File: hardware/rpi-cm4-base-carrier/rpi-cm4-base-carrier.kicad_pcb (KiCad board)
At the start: 4 copper layers, 129.5 x 61.3 mm, 66 parts, among them J1 690-019-298-412, J2 DNP, J3 USB4105-GF-A, J4 SM04B-SRSS-TB(LF)(SN), J5 THD-02-R, J6 Micro_SD_Card_Det, J7 USB_OTG, J8 690-008-221-904, J9 Conn_02x05_Odd_Even, U1 RT9742SNGV, U10 AP22653W6, U2 74LVC1G07SE-7, U3 TPD4EUSB30, U4 TPD4EUSB30, U5 MagJack-A70-112-331N126, U6 RT9742GGJ5, U7 FSUSB42MUX, U8 USB2514B-I/M2, U9 TPD4EUSB30, Y1 CX3225CA24000D0HSSCC

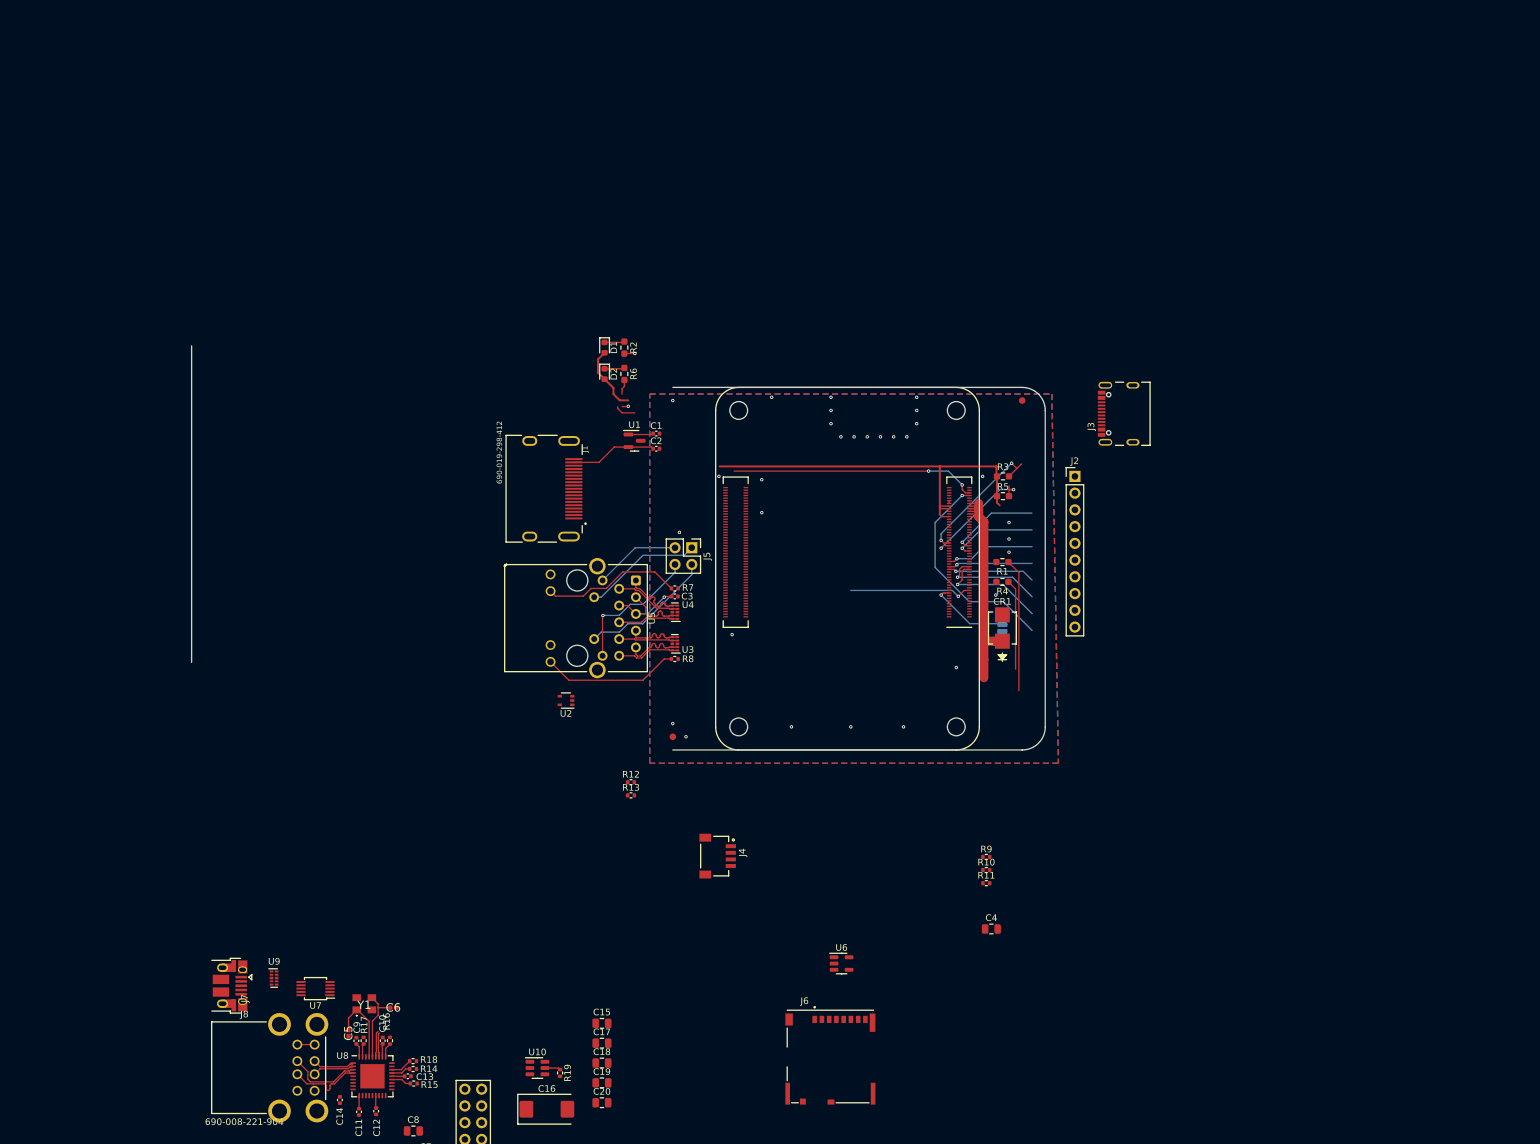
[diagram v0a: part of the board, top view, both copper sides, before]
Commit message: addition of 4xRGB LED's and I2C driver, also includes right angle lightpipe
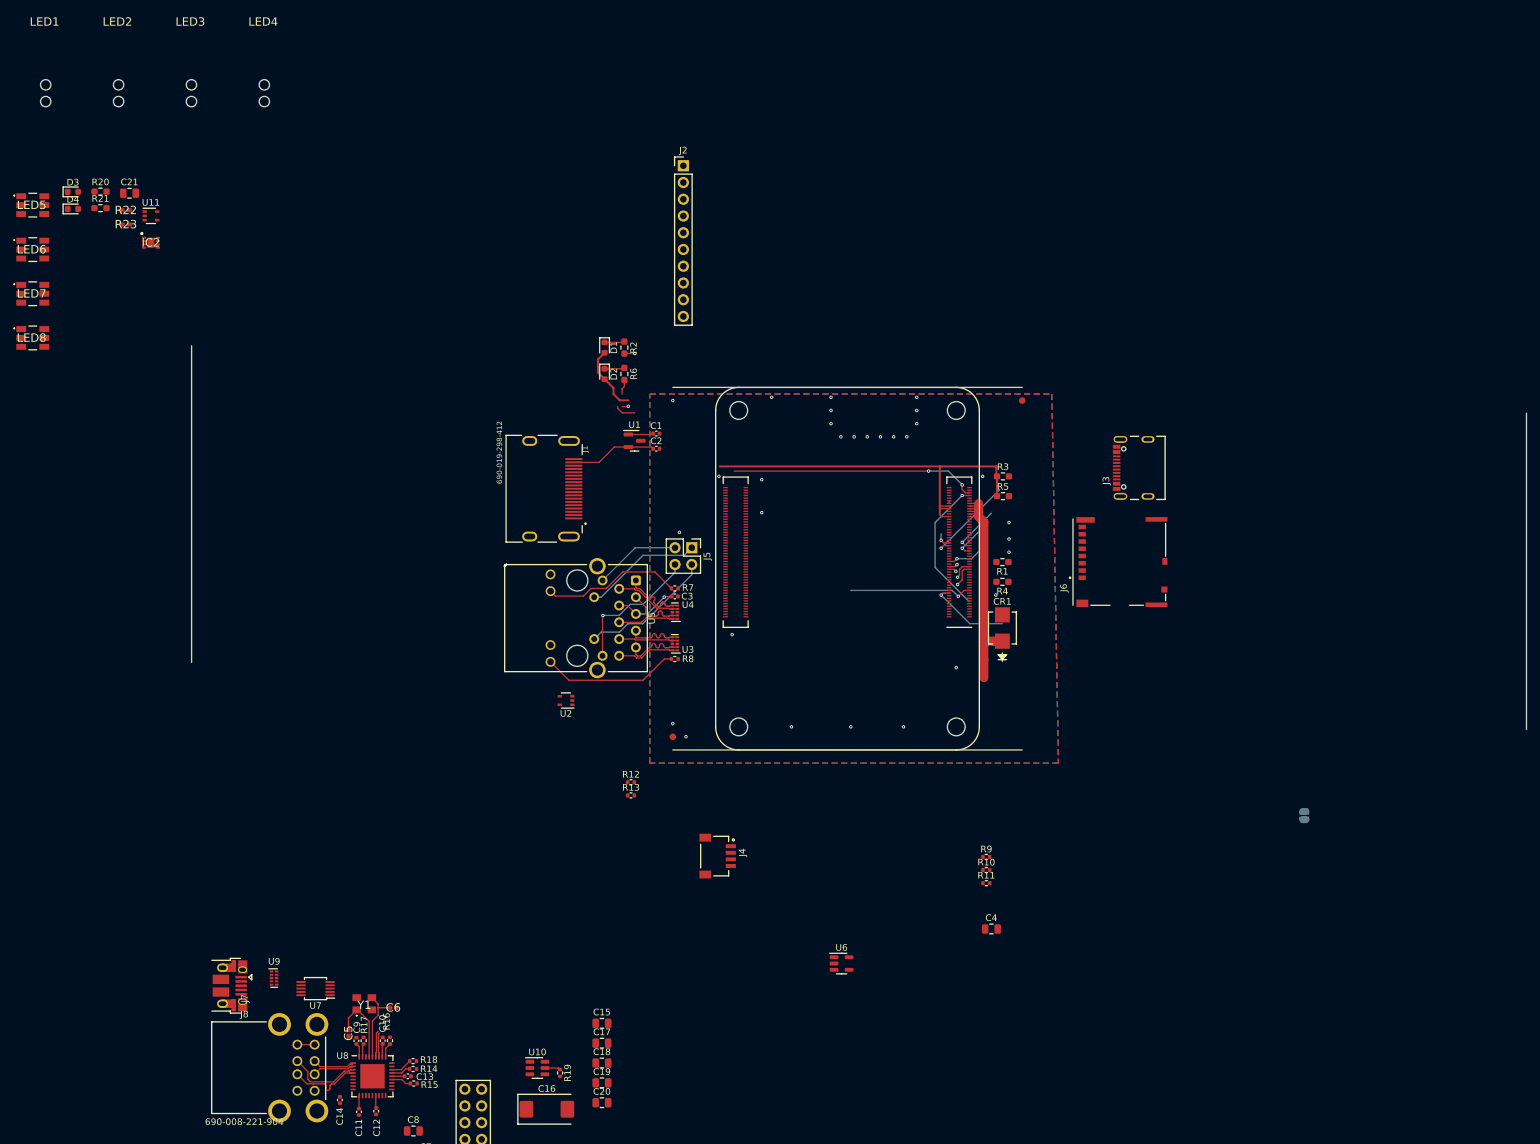
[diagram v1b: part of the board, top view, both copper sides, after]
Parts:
- added C21: 10u, Capacitor_SMD:C_0805_2012Metric, F.Cu at (37.1, 47.5)
- added D3: LED Green, LED_SMD:LED_0603_1608Metric, F.Cu at (28.5, 47.3)
- added D4: LED Red, LED_SMD:LED_0603_1608Metric, F.Cu at (28.5, 49.9)
- added IC2: KTD2052BEVAA-TR, SamacSys_Parts:SON50P200X200X58-9N, F.Cu at (40.3, 55.1)
- added LED1: 515-1114F, SamacSys_Parts:515-1114F, F.Cu at (25.1, 45.3)
- added LED2: 515-1114F, SamacSys_Parts:515-1114F, F.Cu at (36.2, 45.3)
- added LED3: 515-1114F, SamacSys_Parts:515-1114F, F.Cu at (47.2, 45.3)
- added LED4: 515-1114F, SamacSys_Parts:515-1114F, F.Cu at (58.3, 45.3)
- added LED5: APF3236SEEZGKQBKC, SamacSys_Parts:APF3236SEEZGKQBKC, F.Cu at (22.4, 49.4)
- added LED6: APF3236SEEZGKQBKC, SamacSys_Parts:APF3236SEEZGKQBKC, F.Cu at (22.4, 56.1)
- added LED7: APF3236SEEZGKQBKC, SamacSys_Parts:APF3236SEEZGKQBKC, F.Cu at (22.4, 62.8)
- added LED8: APF3236SEEZGKQBKC, SamacSys_Parts:APF3236SEEZGKQBKC, F.Cu at (22.4, 69.5)
- added R20: 1k, Resistor_SMD:R_0603_1608Metric_Pad0.98x0.95mm_HandSolder, F.Cu at (32.7, 47.3)
- added R21: 1k, Resistor_SMD:R_0603_1608Metric_Pad0.98x0.95mm_HandSolder, F.Cu at (32.7, 49.8)
- added R22: 4K7, SamacSys_Parts:RESC1005X37N, F.Cu at (36.5, 50.1)
- added R23: 4K7, SamacSys_Parts:RESC1005X37N, F.Cu at (36.5, 52.3)
- added U11: 74LVC1G07SE-7, Package_TO_SOT_SMD:SOT-353_SC-70-5, F.Cu at (40.3, 51.0)
- moved J6 86.9 mm to (187.2, 103.5), turned to 90 degrees
- moved J2 75.8 mm to (121.1, 43.4)
- moved JP1 53.9 mm to (215.3, 141.9)
- moved J3 8.52 mm to (191.6, 89.2)
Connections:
- J1 pad 10: /CM4 High Speed/HDMI0_CK_P -> /CM4 High Speed/HDMI0_CK_N
- J1 pad 4: /CM4 High Speed/HDMI0_D1_P -> /CM4 High Speed/HDMI0_CK_N
- J1 pad 7: /CM4 High Speed/HDMI0_D0_P -> /CM4 High Speed/HDMI0_CK_N
- J1 pad 9: /CM4 High Speed/HDMI0_D0_N -> /CM4 High Speed/HDMI0_CK_N
- Module1 pad 176: /CM4 High Speed/HDMI0_D1_P -> /CM4 High Speed/HDMI0_CK_N
- Module1 pad 182: /CM4 High Speed/HDMI0_D0_P -> /CM4 High Speed/HDMI0_CK_N
- Module1 pad 184: /CM4 High Speed/HDMI0_D0_N -> /CM4 High Speed/HDMI0_CK_N
- Module1 pad 188: /CM4 High Speed/HDMI0_CK_P -> /CM4 High Speed/HDMI0_CK_N
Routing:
- net Net-(J3-CC1): track 20.2 -> 0.00 mm
- net /CM4 GPIO/GPIO2: track 21.3 -> 2.39 mm, vias 2 -> 1
- net Net-(J3-CC2): track 13.7 -> 0.00 mm
- net /CM4 GPIO/GPIO7: track 16.6 -> 3.51 mm
- net /CM4 GPIO/GPIO8: track 15.5 -> 2.99 mm
- net /CM4 GPIO/GPIO11: track 13.3 -> 1.15 mm
- net /CM4 GPIO/nRPIBOOT: track 32.4 -> 21.0 mm
- net /CM4 GPIO/GPIO9: track 12.8 -> 1.59 mm
- net /CM4 GPIO/GPIO15: track 13.0 -> 5.20 mm
- net /CM4 GPIO/GPIO10: track 13.5 -> 6.15 mm
- net /CM4 GPIO/GPIO14: track 13.7 -> 7.56 mm
- net /CM4 GPIO/GPIO3: track 18.3 -> 14.0 mm, vias 2 -> 1
- net +3V3: track 80.5 -> 79.0 mm
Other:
- board size 129.5 x 61.3 mm -> 202.5 x 61.3 mm

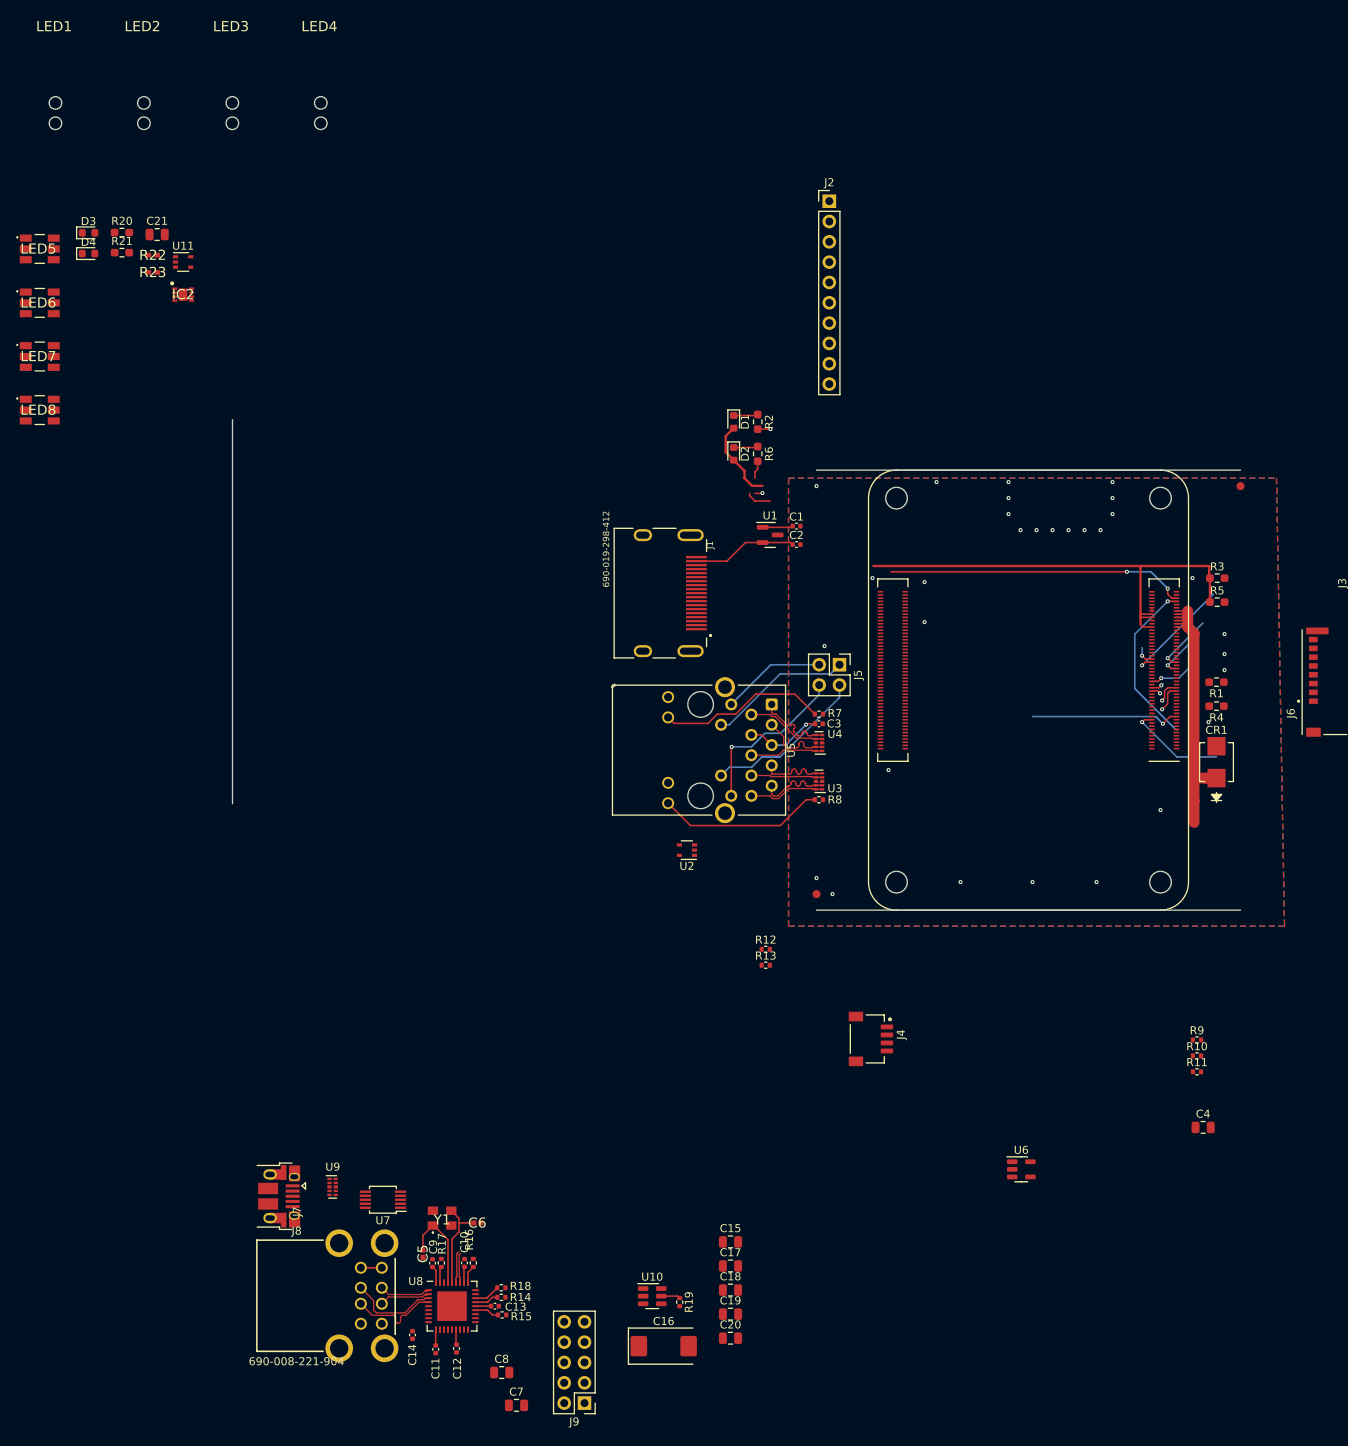
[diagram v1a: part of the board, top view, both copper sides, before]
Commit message: started final placement of blocks, realised ESD suppression devices cannot be manufactured with JLC, need to switch part
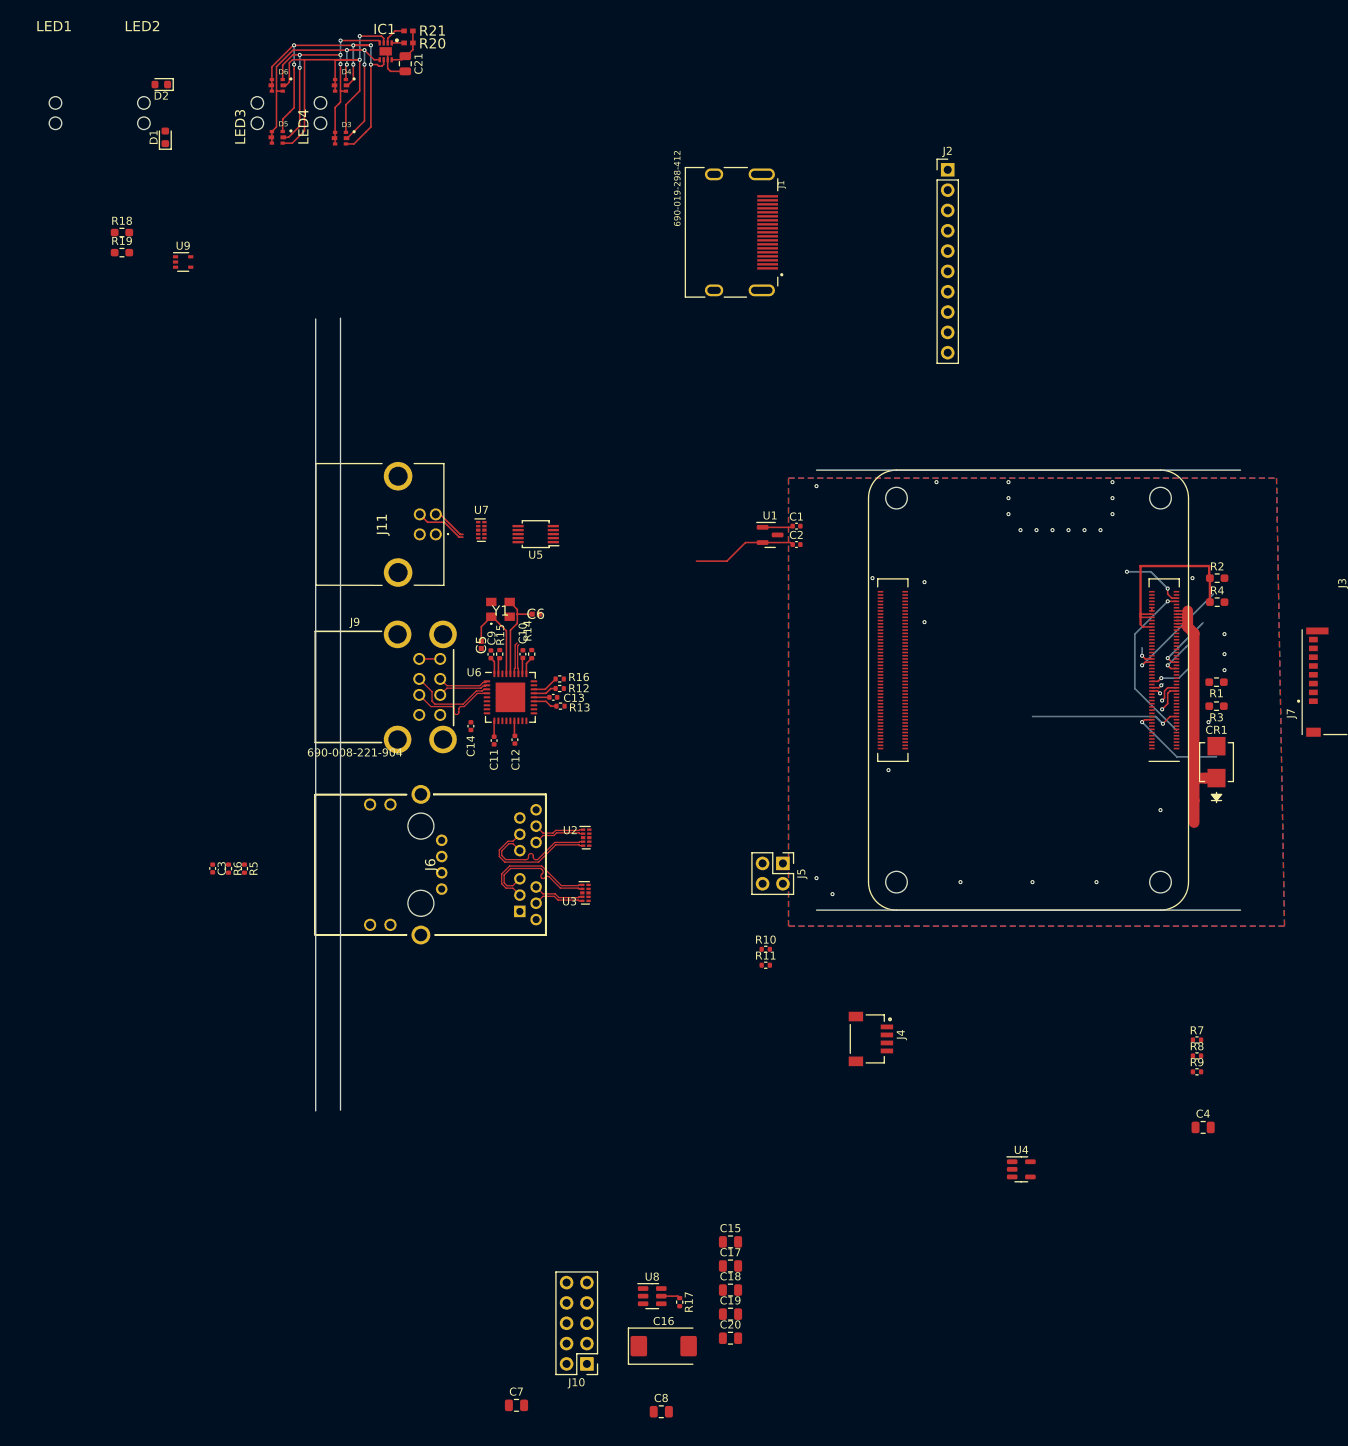
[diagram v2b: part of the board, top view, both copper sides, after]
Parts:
- removed the D1 at (109.2, 71.0)
- removed the D2 at (109.2, 75.0)
- removed IC2: KTD2052BEVAA-TR, SamacSys_Parts:SON50P200X200X58-9N
- removed the J7 at (51.2, 167.8)
- removed LED5, LED6, LED7, LED8: APF3236SEEZGKQBKC, SamacSys_Parts:APF3236SEEZGKQBKC
- removed the R2 at (112.2, 71.0)
- removed the R7 at (119.8, 107.5)
- removed the R8 at (119.8, 118.2)
- removed REF** (x2): Fiducial_1mm_Mask2mm, Fiducial:Fiducial_1mm_Mask2mm
- removed the U2 at (103.3, 124.5)
- removed the U5 at (105.0, 112.0)
- added D3: 19-337C_RSBHGHC-A88_4T, 19_337C_RSBHGHC_A88_4T:LED_19-337C_RSBHGHC-A88_4T, F.Cu at (60.0, 35.5)
- added D4: 19-337C_RSBHGHC-A88_4T, 19_337C_RSBHGHC_A88_4T:LED_19-337C_RSBHGHC-A88_4T, F.Cu at (60.0, 28.9)
- added D5: 19-337C_RSBHGHC-A88_4T, 19_337C_RSBHGHC_A88_4T:LED_19-337C_RSBHGHC-A88_4T, F.Cu at (52.1, 35.4)
- added D6: 19-337C_RSBHGHC-A88_4T, 19_337C_RSBHGHC_A88_4T:LED_19-337C_RSBHGHC-A88_4T, F.Cu at (52.1, 28.9)
- added IC1: KTD2052BEVAA-TR, SamacSys_Parts:SON50P200X200X58-9N, F.Cu at (65.7, 24.6)
- added J11: XM7B-0442, SamacSys_Parts:XM7B0442, F.Cu at (71.9, 85.0)
- added J6: JT4-1202HL, SamacSys_Parts:JT41202HL, F.Cu at (82.4, 132.2)
- added R5: 470R, Resistor_SMD:R_0402_1005Metric, F.Cu at (48.0, 126.8)
- R6: value 1k -> 470R; footprint Resistor_SMD:R_0603_1608Metric_Pad0.98x0.95mm_HandSolder -> Resistor_SMD:R_0402_1005Metric
- moved U5 85.4 mm to (84.4, 85.0)
- moved U7 84.2 mm to (77.6, 84.5)
- moved R6 84.0 mm to (46.0, 126.8)
- moved C3 77.9 mm to (44.0, 126.8), turned to -90 degrees
- moved C11 76.4 mm to (79.2, 110.8)
- moved C12 76.4 mm to (81.8, 110.7)
- moved C9 76.4 mm to (78.8, 100.0)
- moved R12 76.4 mm to (87.4, 104.3)
- moved C10 76.4 mm to (82.8, 100.0)
- moved C13 76.4 mm to (86.6, 105.4)
- moved C14 76.4 mm to (76.3, 109.0)
- moved C5 76.4 mm to (77.6, 98.8)
- moved C6 76.4 mm to (84.4, 95.0)
- moved J9 76.4 mm to (67.1, 104.1)
- moved R13 76.4 mm to (87.5, 106.5)
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- renumbered D3 to D1, D4 to D2, J9 to J10, J6 to J7, J8 to J9, R12 to R10, R13 to R11, R14 to R12, R15 to R13, R16 to R14, R17 to R15, R18 to R16, R19 to R17, R20 to R18, R21 to R19, R3 to R2, R22 to R20, R23 to R21, R4 to R3, R5 to R4, R9 to R7, R10 to R8, R11 to R9, U3 to U2, U4 to U3, U6 to U4, U7 to U5, U8 to U6, U9 to U7, U10 to U8, U11 to U9
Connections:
- C3 pad 1: Net-(C3-Pad1) -> /magjack/TRCT
- Module1 pad 105: /CM4 High Speed/USB2_N -> /CM4 High Speed/USB2_P
- R20 pad 1: /CM4 GPIO/LEDs/SDA -> /CM4 GPIO/SCL0
- R21 pad 1: /CM4 GPIO/LEDs/SCL -> /CM4 GPIO/SDA0
- R6 pad 2: Net-(R6-Pad2) -> /CM4 GPIO/ETH_LEDG
- U2 pad 4: /CM4 GPIO/TRD2_N -> /CM4 GPIO/TRD2_P
- U2 pad 5: /CM4 GPIO/TRD2_P -> /CM4 GPIO/TRD2_N
- U2 pad 6: /CM4 GPIO/TRD2_P -> /CM4 GPIO/TRD2_N
- U2 pad 7: /CM4 GPIO/TRD2_N -> /CM4 GPIO/TRD2_P
- U3 pad 1: /CM4 GPIO/TRD1_N -> /CM4 GPIO/TRD1_P
- U3 pad 10: /CM4 GPIO/TRD1_N -> /CM4 GPIO/TRD1_P
- U3 pad 2: /CM4 GPIO/TRD1_P -> /CM4 GPIO/TRD1_N
- U3 pad 9: /CM4 GPIO/TRD1_P -> /CM4 GPIO/TRD1_N
- U5 pad 3: /CM4 High Speed/USB2_N -> /CM4 High Speed/USB2_P
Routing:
- net /CM4 GPIO/LEDs/RGB1: track 0.00 -> 52.1 mm, vias 0 -> 6
- net /CM4 GPIO/LEDs/RGB3: track 0.00 -> 48.0 mm, vias 0 -> 2
- net /CM4 GPIO/LEDs/RGB2: track 0.00 -> 42.7 mm, vias 0 -> 4
- net /CM4 GPIO/LEDs/RGB4: track 0.00 -> 40.1 mm, vias 0 -> 5
- net +3V3: track 79.0 -> 40.8 mm
- net /CM4 GPIO/nPWR_LED: track 40.6 -> 7.98 mm
- net Net-(U5-LEDG_K): track 21.2 -> 0.00 mm
- net /magjack/TR3_TAP: track 21.0 -> 0.00 mm, vias 1 -> 0
- net Net-(U5-LEDY_K): track 20.8 -> 0.00 mm
- net /magjack/TR2_TAP: track 20.4 -> 0.00 mm
- net /magjack/TR1_TAP: track 17.9 -> 0.00 mm
- net /magjack/TR0_TAP: track 13.0 -> 0.00 mm, vias 1 -> 0
- net Net-(C3-Pad1): track 9.59 -> 0.00 mm, vias 1 -> 0
- net /CM4 GPIO/TRD2_P: track 8.83 -> 15.9 mm
- net /CM4 GPIO/TRD2_N: track 8.93 -> 15.9 mm
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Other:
- board size 202.5 x 61.3 mm -> 192.1 x 99.1 mm
